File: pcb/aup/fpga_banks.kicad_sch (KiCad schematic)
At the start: 1 part, among them U1 XC7A50T-FGG484

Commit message: Update footprints and 3d models. All render
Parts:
- U1: footprint Package_BGA:Xilinx_FGG484 -> !Xilinx:Xilinx_FGG484; Digi-Key Part Number (none) -> 122-2082-ND; LCSC Part # (none) -> C1550658
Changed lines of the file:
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@@
 			)
 		)
-		(property "Footprint" "Package_BGA:Xilinx_FGG484"
+		(property "Footprint" "!Xilinx:Xilinx_FGG484"
 			(at 82.55 92.71 0)
 			(effects
@@
 			)
 		)
-		(property "Description" "Artix 7 T 50 XC7A50T-FGG484"
+		(property "Description" "XC7A50T-2FGG484C"
+			(at 82.55 92.71 0)
+			(effects
+				(font
+					(size 1.27 1.27)
+				)
+				(hide yes)
+			)
+		)
+		(property "LCSC Part #" "C1550658"
+			(at 82.55 92.71 0)
+			(effects
+				(font
+					(size 1.27 1.27)
+				)
+				(hide yes)
+			)
+		)
+		(property "Digi-Key Part Number" "122-2082-ND"
 			(at 82.55 92.71 0)
 			(effects
@@
 			)
 		)
-		(property "Footprint" "Package_BGA:Xilinx_FGG484"
+		(property "Footprint" "!Xilinx:Xilinx_FGG484"
 			(at 201.93 93.98 0)
 			(effects
@@
 			)
 		)
-		(property "Description" "Artix 7 T 50 XC7A50T-FGG484"
+		(property "Description" "XC7A50T-2FGG484C"
+			(at 201.93 93.98 0)
+			(effects
+				(font
+					(size 1.27 1.27)
+				)
+				(hide yes)
+			)
+		)
+		(property "LCSC Part #" "C1550658"
+			(at 201.93 93.98 0)
+			(effects
+				(font
+					(size 1.27 1.27)
+				)
+				(hide yes)
+			)
+		)
+		(property "Digi-Key Part Number" "122-2082-ND"
 			(at 201.93 93.98 0)
 			(effects
@@
 			)
 		)
-		(property "Footprint" "Package_BGA:Xilinx_FGG484"
+		(property "Footprint" "!Xilinx:Xilinx_FGG484"
 			(at 76.2 210.82 0)
 			(effects
@@
 			)
 		)
-		(property "Description" "Artix 7 T 50 XC7A50T-FGG484"
+		(property "Description" "XC7A50T-2FGG484C"
+			(at 76.2 210.82 0)
+			(effects
+				(font
+					(size 1.27 1.27)
+				)
+				(hide yes)
+			)
+		)
+		(property "LCSC Part #" "C1550658"
+			(at 76.2 210.82 0)
+			(effects
+				(font
+					(size 1.27 1.27)
+				)
+				(hide yes)
+			)
+		)
+		(property "Digi-Key Part Number" "122-2082-ND"
 			(at 76.2 210.82 0)
 			(effects
@@
 			)
 		)
-		(property "Footprint" "Package_BGA:Xilinx_FGG484"
+		(property "Footprint" "!Xilinx:Xilinx_FGG484"
 			(at 317.5 92.71 0)
 			(effects
@@
 			)
 		)
-		(property "Description" "Artix 7 T 50 XC7A50T-FGG484"
+		(property "Description" "XC7A50T-2FGG484C"
 			(at 317.5 92.71 0)
 			(effects
+				(font
+					(size 1.27 1.27)
+				)
+				(hide yes)
+			)
+		)
+		(property "LCSC Part #" "C1550658"
+			(at 317.5 92.71 0)
+			(effects
+				(font
+					(size 1.27 1.27)
+				)
+				(hide yes)
+			)
+		)
+		(property "Digi-Key Part Number" "122-2082-ND"
+			(at 317.5 92.71 0)
+			(effects

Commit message: Cleanup power layout
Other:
- moved on the sheet: U1A

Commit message: Very rough assigment for DDR to banks
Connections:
- net DDR_DM1: now reaches U1.AA1 (IO_L7P_T1_34)
- net DDR_UQDS_N: now reaches U1.AA3 (IO_L9N_T1_DQS_34)
- net DDR_DQ15: now reaches U1.AA4 (IO_L11N_T1_SRCC_34)
- net DDR_DQ10: now reaches U1.AA5 (IO_L10P_T1_34)
- net DDR_A12: now reaches U1.AA6 (IO_L18N_T2_34)
- net DDR_DQ3: now reaches U1.AA8 (IO_L22P_T3_34)
- net DDR_DQ14: now reaches U1.AB1 (IO_L7N_T1_34)
- net DDR_DQ9: now reaches U1.AB2 (IO_L8N_T1_34)
- net DDR_DQ11: now reaches U1.AB3 (IO_L8P_T1_34)
- net DDR_DQ12: now reaches U1.AB5 (IO_L10N_T1_34)
- net DDR_DQ1: now reaches U1.AB6 (IO_L20N_T3_34)
- net DDR_DQ4: now reaches U1.AB7 (IO_L20P_T3_34)
- net DDR_DQ6: now reaches U1.AB8 (IO_L22N_T3_34)
- net DDR_A7: now reaches U1.R2 (IO_L3N_T0_DQS_34)
- net DDR_WE: now reaches U1.R3 (IO_L3P_T0_DQS_34)
- net DDR_A9: now reaches U1.R4 (IO_L13P_T2_MRCC_34)
- net DDR_BA2: now reaches U1.R6 (IO_L17P_T2_34)
- net DDR_CAS: now reaches U1.T1 (IO_L1P_T0_34)
- net DDR_CS: now reaches U1.T3 (IO_0_34)
- net DDR_A5: now reaches U1.T4 (IO_L13N_T2_MRCC_34)
- net DDR_A1: now reaches U1.T5 (IO_L14P_T2_SRCC_34)
- net DDR_A3: now reaches U1.T6 (IO_L17N_T2_34)
- net DDR_CKE: now reaches U1.U1 (IO_L1N_T0_34)
- net DDR_A13: now reaches U1.U2 (IO_L2P_T0_34)
- net DDR_CK_P: now reaches U1.U3 (IO_L6P_T0_34)
- net DDR_BA1: now reaches U1.U5 (IO_L14N_T2_SRCC_34)
- net DDR_A0: now reaches U1.U6 (IO_L16P_T2_34)
- net DDR_RST: now reaches U1.U7 (IO_25_34)
- net DDR_A4: now reaches U1.V2 (IO_L2N_T0_34)
- net DDR_CK_N: now reaches U1.V3 (IO_L6N_T0_VREF_34)
- net DDR_DQ8: now reaches U1.V4 (IO_L12P_T1_MRCC_34)
- net DDR_RAS: now reaches U1.V5 (IO_L16N_T2_34)
- net DDR_DQ5: now reaches U1.V7 (IO_L19P_T3_34)
- net DDR_LDQS_N: now reaches U1.V8 (IO_L21N_T3_DQS_34)
- net DDR_LDQS_P: now reaches U1.V9 (IO_L21P_T3_DQS_34)
- net DDR_A8: now reaches U1.W1 (IO_L5P_T0_34)
- net DDR_ODT: now reaches U1.W2 (IO_L4P_T0_34)
- net DDR_DQ13: now reaches U1.W4 (IO_L12N_T1_MRCC_34)
- net DDR_A10: now reaches U1.W5 (IO_L15N_T2_DQS_34)
- net DDR_BA0: now reaches U1.W6 (IO_L15P_T2_DQS_34)
- net DDR_DQ7: now reaches U1.W7 (IO_L19N_T3_VREF_34)
- net DDR_DQ2: now reaches U1.W9 (IO_L24P_T3_34)
- net DDR_A11: now reaches U1.Y1 (IO_L5N_T0_34)
- net DDR_A6: now reaches U1.Y2 (IO_L4N_T0_34)
- net DDR_UDQS_P: now reaches U1.Y3 (IO_L9P_T1_DQS_34)
- net DDR_A2: now reaches U1.Y6 (IO_L18P_T2_34)
- net DDR_DM0: now reaches U1.Y7 (IO_L23N_T3_34)
- net DDR_DQ0: now reaches U1.Y8 (IO_L23P_T3_34)
- no-connect marks 0 -> 2
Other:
- moved on the sheet: U1A, U1B, U1C, U1D

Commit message: All rails assigned net classes
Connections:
- net +3V3: now reaches U1.AA17 (VCCO_13)
- net +3V3: now also U1.AB14 (VCCO_13), U1.C1 (VCCO_35), U1.F2 (VCCO_35), U1.H6 (VCCO_35), U1.J3 (VCCO_35), U1.M14 (VCCO_14), U1.M4 (VCCO_35), U1.N1 (VCCO_35), U1.P18 (VCCO_14), U1.R15 (VCCO_14), U1.T22 (VCCO_14), U1.U19 (VCCO_14), U1.V16 (VCCO_13), U1.W13 (VCCO_13), U1.Y10 (VCCO_13), U1.Y20 (VCCO_14)
- net +Vsel: now reaches U1.A17 (VCCO_16)
- net +Vsel: now also U1.B14 (VCCO_16), U1.C21 (VCCO_16), U1.D18 (VCCO_16), U1.E15 (VCCO_16), U1.F22 (VCCO_16), U1.G19 (VCCO_15), U1.H16 (VCCO_15), U1.J13 (VCCO_15), U1.K20 (VCCO_15), U1.L17 (VCCO_15), U1.N21 (VCCO_15)
- net +1V35: now reaches U1.AA7 (VCCO_34)
- net +1V35: now also U1.AB4 (VCCO_34), U1.R5 (VCCO_34), U1.T2 (VCCO_34), U1.V6 (VCCO_34), U1.W3 (VCCO_34)
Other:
- moved on the sheet: U1C, U1D

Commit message: IO bank netclass assignments
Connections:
- net at U1.A10 (MGTPRXN2_216): now also U1.A4 (MGTPTXN0_216), U1.A6 (MGTPTXN2_216), U1.A8 (MGTPRXN0_216), U1.B10 (MGTPRXP2_216), U1.B4 (MGTPTXP0_216), U1.B6 (MGTPTXP2_216), U1.B8 (MGTPRXP0_216), U1.C11 (MGTPRXN1_216), U1.C5 (MGTPTXN1_216), U1.C7 (MGTPTXN3_216), U1.C9 (MGTPRXN3_216), U1.D11 (MGTPRXP1_216), U1.D5 (MGTPTXP1_216), U1.D7 (MGTPTXP3_216), U1.D9 (MGTPRXP3_216)
- net at U1.AA18 (IO_L17P_T2_A14_D30_14): now also U1.AA19 (IO_L15P_T2_DQS_RDWR_B_14), U1.AA20 (IO_L8P_T1_D11_14), U1.AA21 (IO_L8N_T1_D12_14), U1.AB18 (IO_L17N_T2_A13_D29_14), U1.AB20 (IO_L15N_T2_DQS_DOUT_CSO_B_14), U1.AB21 (IO_L10P_T1_D14_14), U1.AB22 (IO_L10N_T1_D15_14), U1.N13 (IO_L23P_T3_A03_D19_14), U1.N14 (IO_L23N_T3_A02_D18_14), U1.N15 (IO_25_14), U1.N17 (IO_L21P_T3_DQS_14), U1.P14 (IO_L19P_T3_A10_D26_14), U1.P15 (IO_L22P_T3_A05_D21_14), U1.P16 (IO_L24P_T3_A01_D17_14), U1.P17 (IO_L21N_T3_DQS_A06_D22_14), U1.P19 (IO_L5P_T0_D06_14), U1.P20 (IO_0_14), U1.P21 (IO_L2P_T0_D02_14), U1.P22 (IO_L1P_T0_D00_MOSI_14), U1.R14 (IO_L19N_T3_A09_D25_VREF_14), U1.R16 (IO_L22N_T3_A04_D20_14), U1.R17 (IO_L24N_T3_A00_D16_14), U1.R18 (IO_L20P_T3_A08_D24_14), U1.R19 (IO_L5N_T0_D07_14), U1.R21 (IO_L2N_T0_D03_14), U1.R22 (IO_L1N_T0_D01_DIN_14), U1.T18 (IO_L20N_T3_A07_D23_14), U1.T19 (IO_L6P_T0_FCS_B_14), U1.T20 (IO_L6N_T0_D08_VREF_14), U1.T21 (IO_L4P_T0_D04_14), U1.U17 (IO_L18P_T2_A12_D28_14), U1.U18 (IO_L18N_T2_A11_D27_14), U1.U20 (IO_L11P_T1_SRCC_14), U1.U21 (IO_L4N_T0_D05_14), U1.U22 (IO_L3P_T0_DQS_PUDC_B_14), U1.V17 (IO_L16P_T2_CSI_B_14), U1.V18 (IO_L14P_T2_SRCC_14), U1.V19 (IO_L14N_T2_SRCC_14), U1.V20 (IO_L11N_T1_SRCC_14), U1.V22 (IO_L3N_T0_DQS_EMCCLK_14), U1.W17 (IO_L16N_T2_A15_D31_14), U1.W19 (IO_L12P_T1_MRCC_14), U1.W20 (IO_L12N_T1_MRCC_14), U1.W21 (IO_L7P_T1_D09_14), U1.W22 (IO_L7N_T1_D10_14), U1.Y18 (IO_L13P_T2_MRCC_14), U1.Y19 (IO_L13N_T2_MRCC_14), U1.Y21 (IO_L9P_T1_DQS_14), U1.Y22 (IO_L9N_T1_DQS_D13_14)
- net at U1.A13 (IO_L10P_T1_16): now also U1.A14 (IO_L10N_T1_16), U1.A15 (IO_L9P_T1_DQS_16), U1.A16 (IO_L9N_T1_DQS_16), U1.A18 (IO_L17P_T2_16), U1.A19 (IO_L17N_T2_16), U1.A20 (IO_L16N_T2_16), U1.A21 (IO_L21N_T3_DQS_16), U1.B13 (IO_L8N_T1_16), U1.B15 (IO_L7P_T1_16), U1.B16 (IO_L7N_T1_16), U1.B17 (IO_L11P_T1_SRCC_16), U1.B18 (IO_L11N_T1_SRCC_16), U1.B20 (IO_L16P_T2_16), U1.B21 (IO_L21P_T3_DQS_16), U1.B22 (IO_L20N_T3_16), U1.C13 (IO_L8P_T1_16), U1.C14 (IO_L3P_T0_DQS_16), U1.C15 (IO_L3N_T0_DQS_16), U1.C17 (IO_L12N_T1_MRCC_16), U1.C18 (IO_L13P_T2_MRCC_16), U1.C19 (IO_L13N_T2_MRCC_16), U1.C20 (IO_L19N_T3_VREF_16), U1.C22 (IO_L20P_T3_16), U1.D14 (IO_L6P_T0_16), U1.D15 (IO_L6N_T0_VREF_16), U1.D16 (IO_L5N_T0_16), U1.D17 (IO_L12P_T1_MRCC_16), U1.D19 (IO_L14N_T2_SRCC_16), U1.D20 (IO_L19P_T3_16), U1.D21 (IO_L23N_T3_16), U1.D22 (IO_L22N_T3_16), U1.E13 (IO_L4P_T0_16), U1.E14 (IO_L4N_T0_16), U1.E16 (IO_L5P_T0_16), U1.E17 (IO_L2N_T0_16), U1.E18 (IO_L15N_T2_DQS_16), U1.E19 (IO_L14P_T2_SRCC_16), U1.E21 (IO_L23P_T3_16), U1.E22 (IO_L22P_T3_16), U1.F13 (IO_L1P_T0_16), U1.F14 (IO_L1N_T0_16), U1.F15 (IO_0_16), U1.F16 (IO_L2P_T0_16), U1.F18 (IO_L15P_T2_DQS_16), U1.F19 (IO_L18P_T2_16), U1.F20 (IO_L18N_T2_16), U1.F21 (IO_25_16), U1.G21 (IO_L24P_T3_16), U1.G22 (IO_L24N_T3_16)
- net at U1.G13 (IO_L1N_T0_AD0N_15): now also U1.G15 (IO_L2P_T0_AD8P_15), U1.G16 (IO_L2N_T0_AD8N_15), U1.G17 (IO_L4P_T0_15), U1.G18 (IO_L4N_T0_15), U1.G20 (IO_L8N_T1_AD10N_15), U1.H13 (IO_L1P_T0_AD0P_15), U1.H14 (IO_L3N_T0_DQS_AD1N_15), U1.H15 (IO_L5N_T0_AD9N_15), U1.H17 (IO_L6P_T0_15), U1.H18 (IO_L6N_T0_VREF_15), U1.H19 (IO_L12N_T1_MRCC_15), U1.H20 (IO_L8P_T1_AD10P_15), U1.H22 (IO_L7N_T1_AD2N_15), U1.J14 (IO_L3P_T0_DQS_AD1P_15), U1.J15 (IO_L5P_T0_AD9P_15), U1.J16 (IO_0_15), U1.J17 (IO_L21N_T3_DQS_A18_15), U1.J19 (IO_L12P_T1_MRCC_15), U1.J20 (IO_L11P_T1_SRCC_15), U1.J21 (IO_L11N_T1_SRCC_15), U1.J22 (IO_L7P_T1_AD2P_15), U1.K13 (IO_L19P_T3_A22_15), U1.K14 (IO_L19N_T3_A21_VREF_15), U1.K16 (IO_L23N_T3_FWE_B_15), U1.K17 (IO_L21P_T3_DQS_15), U1.K18 (IO_L13P_T2_MRCC_15), U1.K19 (IO_L13N_T2_MRCC_15), U1.K21 (IO_L9P_T1_DQS_AD3P_15), U1.K22 (IO_L9N_T1_DQS_AD3N_15), U1.L13 (IO_L20N_T3_A19_15), U1.L14 (IO_L22P_T3_A17_15), U1.L15 (IO_L22N_T3_A16_15), U1.L16 (IO_L23P_T3_FOE_B_15), U1.L18 (IO_L16N_T2_A27_15), U1.L19 (IO_L14P_T2_SRCC_15), U1.L20 (IO_L14N_T2_SRCC_15), U1.L21 (IO_L10N_T1_AD11N_15), U1.M13 (IO_L20P_T3_A20_15), U1.M15 (IO_L24P_T3_RS1_15), U1.M16 (IO_L24N_T3_RS0_15), U1.M17 (IO_25_15), U1.M18 (IO_L16P_T2_A28_15), U1.M20 (IO_L18N_T2_A23_15), U1.M21 (IO_L10P_T1_AD11P_15), U1.M22 (IO_L15N_T2_DQS_ADV_B_15), U1.N18 (IO_L17P_T2_A26_15), U1.N19 (IO_L17N_T2_A25_15), U1.N20 (IO_L18P_T2_A24_15), U1.N22 (IO_L15P_T2_DQS_15)
- net at U1.A1 (IO_L1N_T0_AD4N_35): now also U1.B1 (IO_L1P_T0_AD4P_35), U1.B2 (IO_L2N_T0_AD12N_35), U1.C2 (IO_L2P_T0_AD12P_35), U1.D1 (IO_L3N_T0_DQS_AD5N_35), U1.D2 (IO_L4N_T0_35), U1.E1 (IO_L3P_T0_DQS_AD5P_35), U1.E2 (IO_L4P_T0_35), U1.E3 (IO_L6N_T0_VREF_35), U1.F1 (IO_L5N_T0_AD13N_35), U1.F3 (IO_L6P_T0_35), U1.F4 (IO_0_35), U1.G1 (IO_L5P_T0_AD13P_35), U1.G2 (IO_L8N_T1_AD14N_35), U1.G3 (IO_L11N_T1_SRCC_35), U1.G4 (IO_L12N_T1_MRCC_35), U1.H2 (IO_L8P_T1_AD14P_35), U1.H3 (IO_L11P_T1_SRCC_35), U1.H4 (IO_L12P_T1_MRCC_35), U1.H5 (IO_L10N_T1_AD15N_35), U1.J1 (IO_L7N_T1_AD6N_35), U1.J2 (IO_L9N_T1_DQS_AD7N_35), U1.J4 (IO_L13N_T2_MRCC_35), U1.J5 (IO_L10P_T1_AD15P_35), U1.J6 (IO_L17N_T2_35), U1.K1 (IO_L7P_T1_AD6P_35), U1.K2 (IO_L9P_T1_DQS_AD7P_35), U1.K3 (IO_L14N_T2_SRCC_35), U1.K4 (IO_L13P_T2_MRCC_35), U1.K6 (IO_L17P_T2_35), U1.L1 (IO_L15N_T2_DQS_35), U1.L3 (IO_L14P_T2_SRCC_35), U1.L4 (IO_L18N_T2_35), U1.L5 (IO_L18P_T2_35), U1.L6 (IO_25_35), U1.M1 (IO_L15P_T2_DQS_35), U1.M2 (IO_L16N_T2_35), U1.M3 (IO_L16P_T2_35), U1.M5 (IO_L23N_T3_35), U1.M6 (IO_L23P_T3_35), U1.N2 (IO_L22N_T3_35), U1.N3 (IO_L19N_T3_VREF_35), U1.N4 (IO_L19P_T3_35), U1.N5 (IO_L24N_T3_35), U1.P1 (IO_L20N_T3_35), U1.P2 (IO_L22P_T3_35), U1.P4 (IO_L21N_T3_DQS_35), U1.P5 (IO_L21P_T3_DQS_35), U1.P6 (IO_L24P_T3_35), U1.R1 (IO_L20P_T3_35)
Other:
- moved on the sheet: U1B

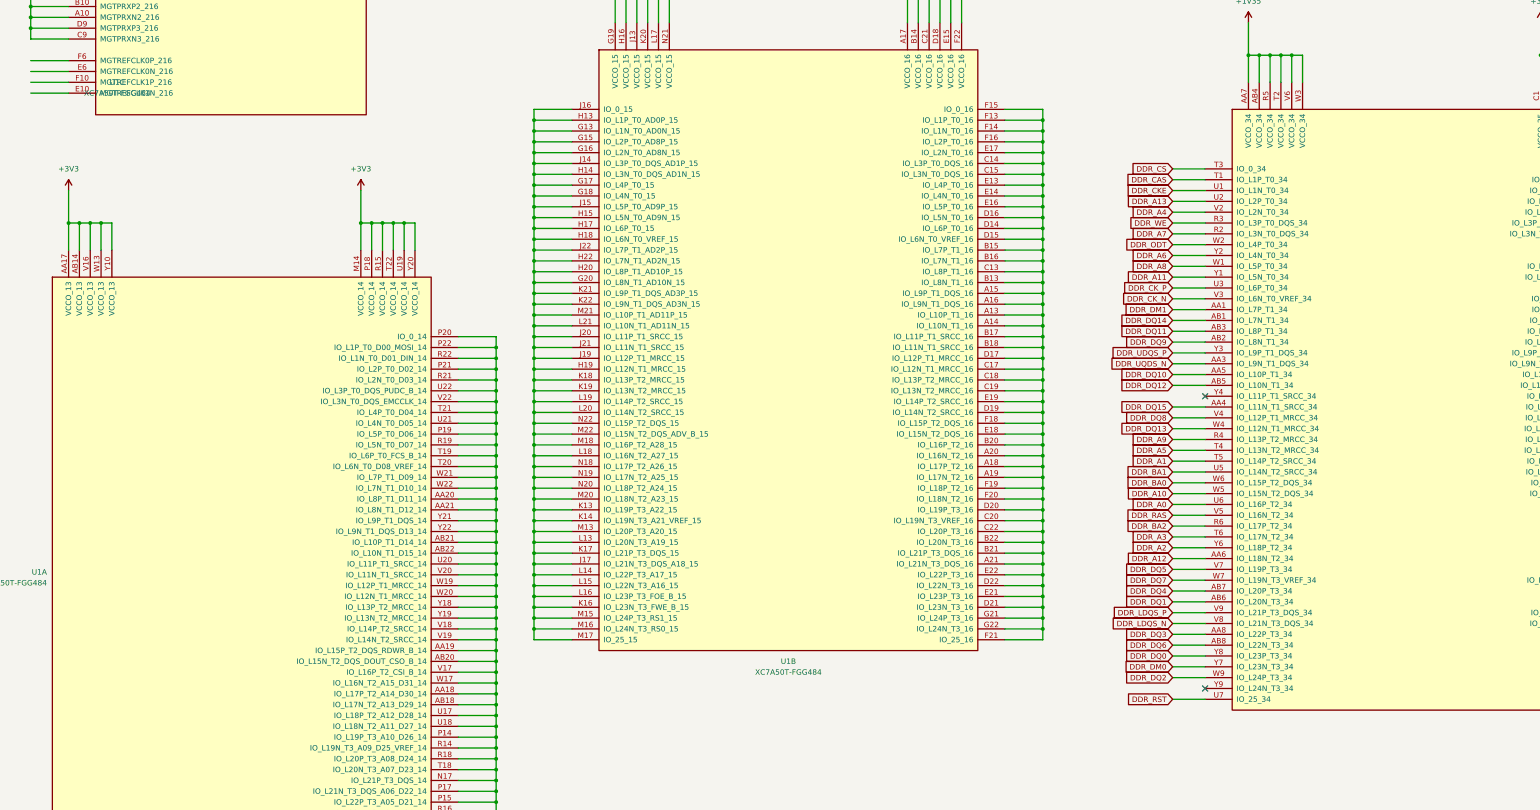
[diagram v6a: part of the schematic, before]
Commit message: Align fpga in daughter area
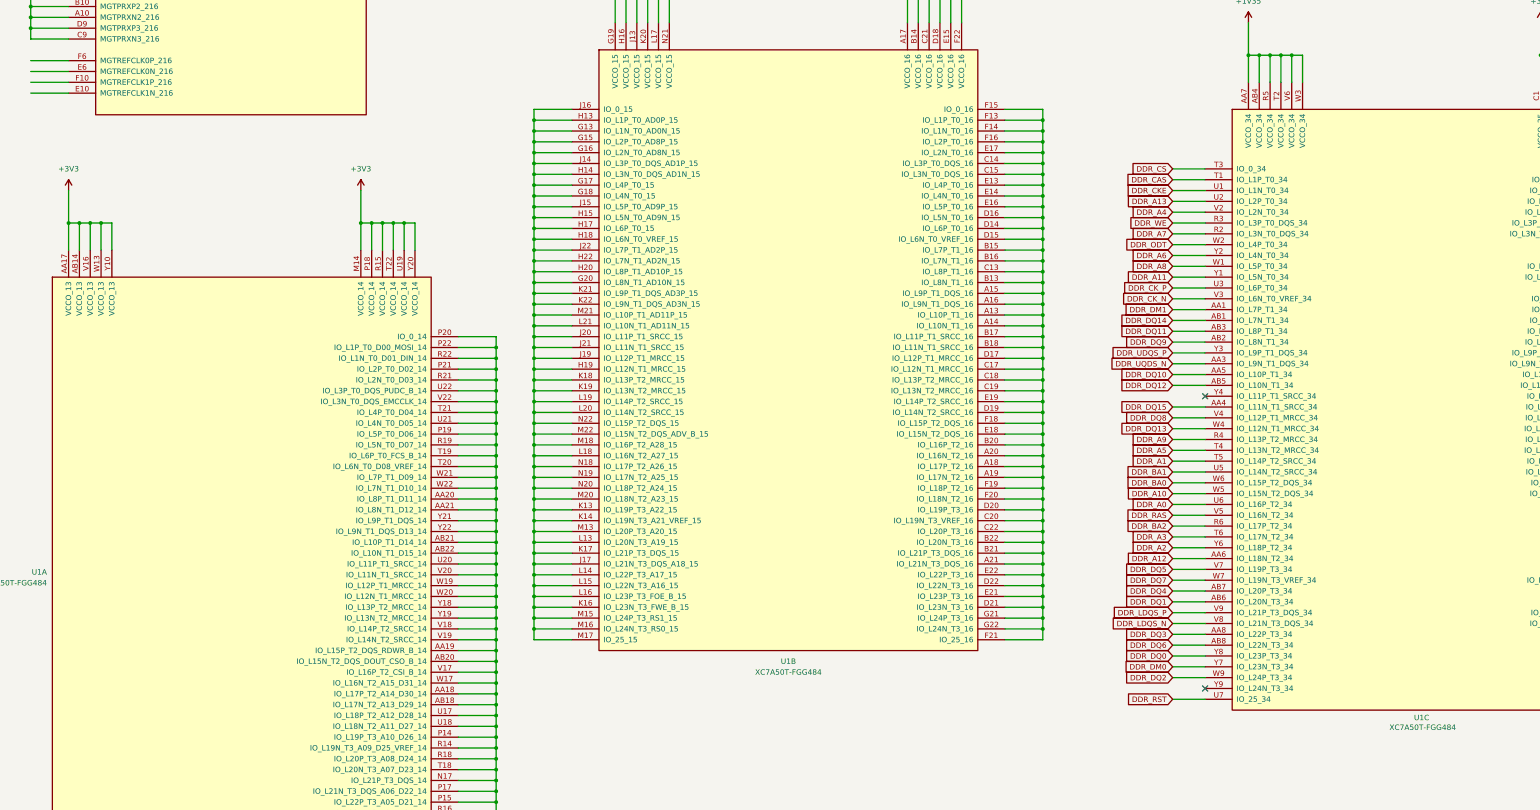
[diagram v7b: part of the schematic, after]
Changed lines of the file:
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@@
 		(dnp no)
 		(property "Reference" "U1"
-			(at 43.18 76.2 0)
+			(at 349.25 225.298 0)
 			(effects
 				(font
@@
 		)
 		(property "Value" "XC7A50T-FGG484"
-			(at 43.18 78.74 0)
+			(at 349.504 227.584 0)
 			(effects
 				(font
